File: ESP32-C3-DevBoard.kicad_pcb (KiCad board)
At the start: 2 copper layers, 25.4 x 26 mm, 21 parts, among them J1 USB_C_Receptacle_USB2.0, J2 Conn_01x10, J3 Conn_01x10, SW1 SW_Push, SW2 SW_Push, U1 ESP32-C3-WROOM-02, U3 RT9080-33GJ5

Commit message: Add files via upload
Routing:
- net Net-(J1-CC2): track 11.0 -> 11.7 mm

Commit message: Add files via upload
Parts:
- C3: value 100nF -> 1uF
- C4: value 100nF -> 0.1uF
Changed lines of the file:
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@@
         (effects (font (size 1 1) (thickness 0.15)))
     )
-    (fp_text value "100nF" (at 0 1.16) (layer "F.Fab")
+    (fp_text value "0.1uF" (at 0 1.16) (layer "F.Fab")
         (effects (font (size 1 1) (thickness 0.15)))
     )
@@
     (descr "Capacitor SMD 0402 (1005 Metric), square (rectangular) end terminal, IPC_7351 nominal, (Body size source: IPC-SM-782 page 76, https://www.pcb-3d.com/wordpress/wp-content/uploads/ipc-sm-782a_amendment_1_and_2.pdf), generated with kicad-footprint-generator")
     (tags "capacitor")
-    (property "LCSC" "C1525")
+    (property "LCSC" "C52923")
     (property "Sheetfile" "ESP32-C3-DevBoard.kicad_sch")
     (property "Sheetname" "")
@@
         (effects (font (size 1 1) (thickness 0.15)))
     )
-    (fp_text value "100nF" (at 0 1.16) (layer "F.Fab")
-        (effects (font (size 1 1) (thickness 0.15)))
-    )
+    (fp_text value "1uF" (at 0 1.16) (layer "F.Fab")
+        (effects (font (size 1 1) (thickness 0.15)))
+    )

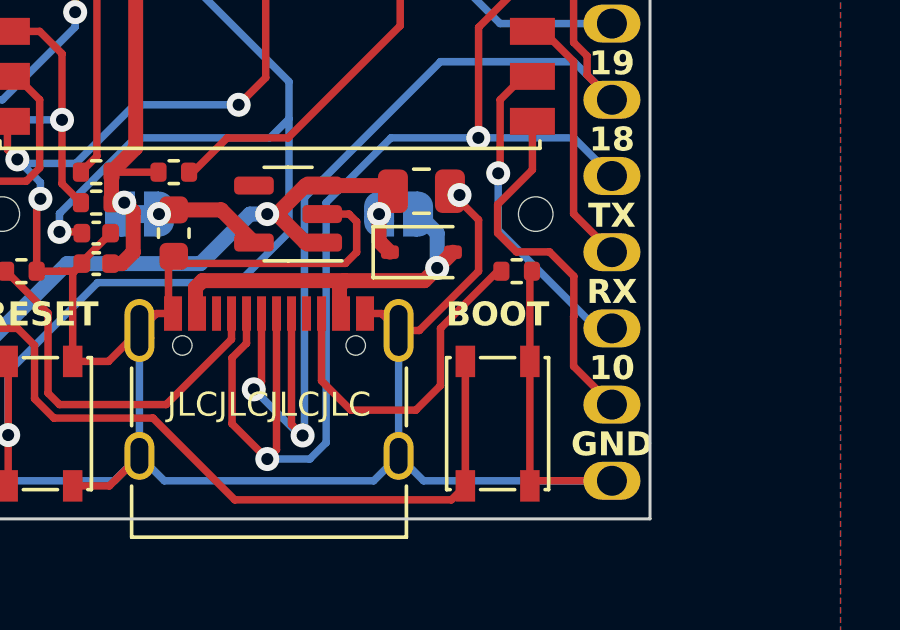
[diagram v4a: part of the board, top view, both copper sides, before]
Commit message: KiCAD 8.0
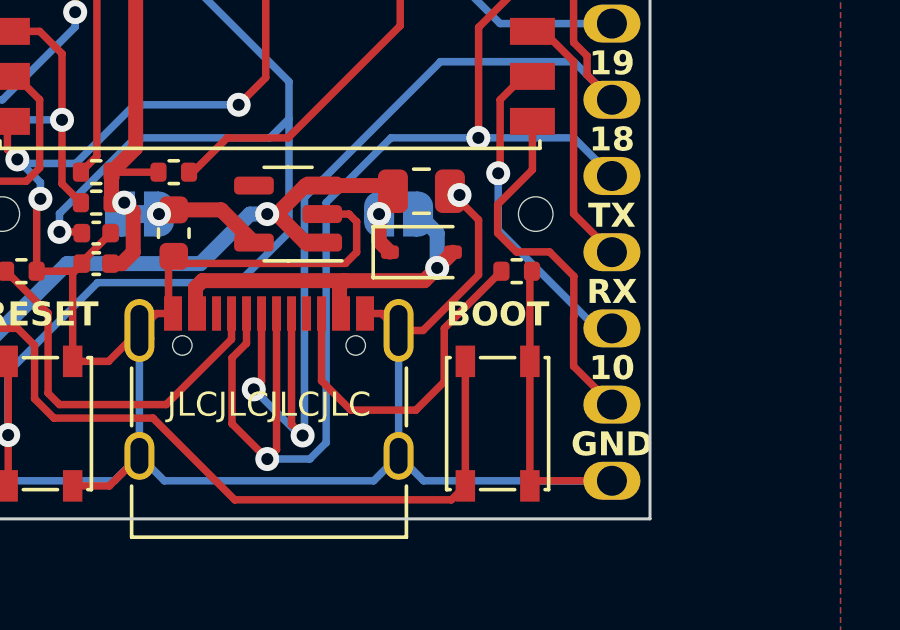
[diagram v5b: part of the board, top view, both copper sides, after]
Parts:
- J1: value USB_C_Receptacle_USB2.0 -> USB_C_Receptacle_USB2.0_16P
